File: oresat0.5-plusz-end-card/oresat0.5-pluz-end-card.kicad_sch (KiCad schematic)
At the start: 30 parts, among them J1 J-SAMTEC-TFM-120-01-L-D-RA, J2 Harwin M55-7101242R, J3 Harwin M55-7101242R, J4 Harwin M55-7101242R, J5 Harwin M55-7101242R, J6 Conn_Coaxial

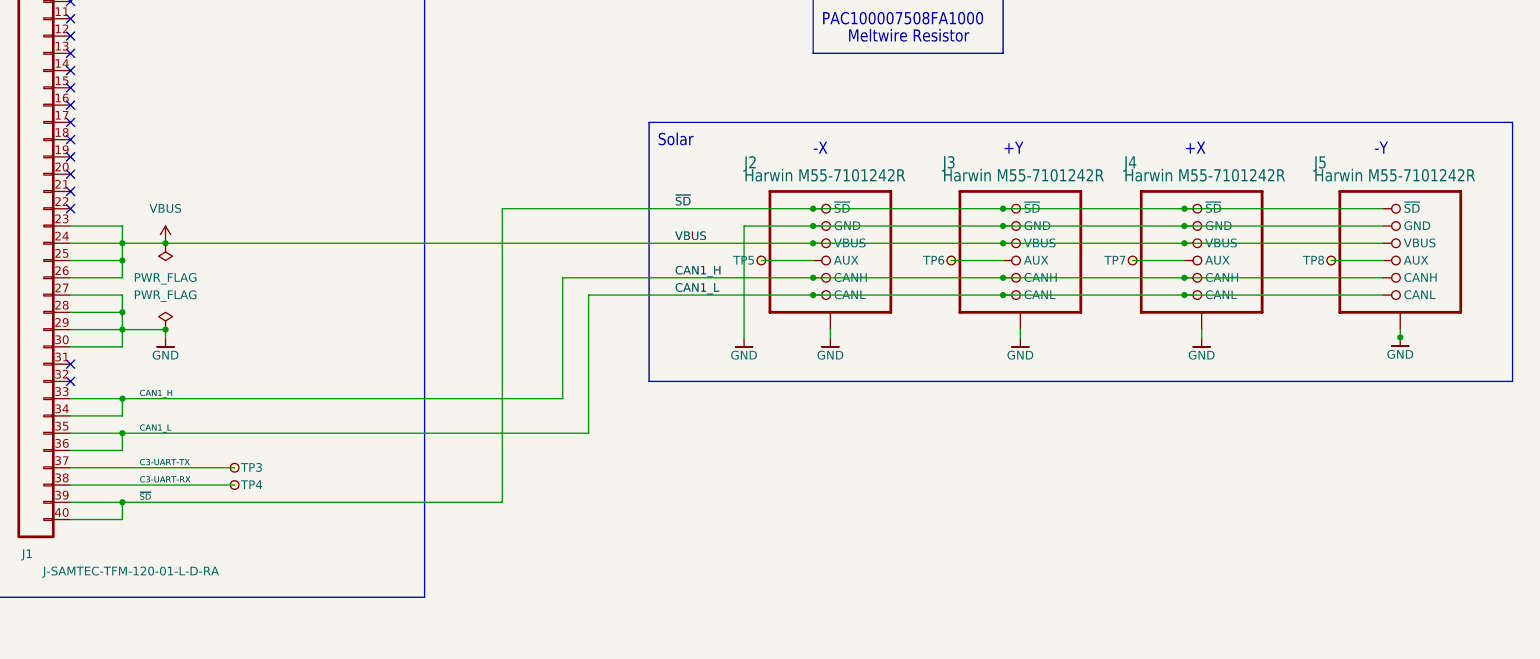
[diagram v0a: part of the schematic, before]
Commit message: Updated +Z end card connector symbols
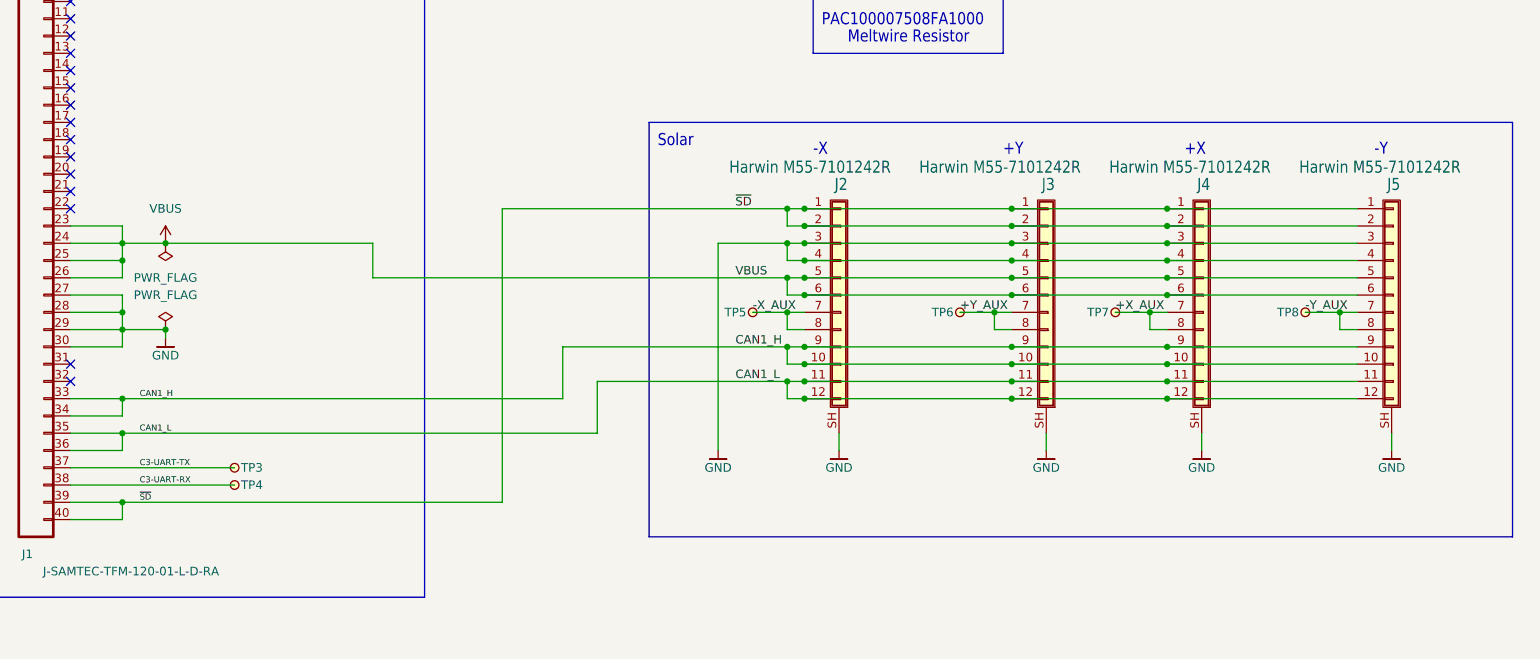
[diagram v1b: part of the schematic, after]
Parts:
- CF1: footprint plusz-end-card-with-turnstile:HARWIN-M55-60X1242R -> oresat-connectors:J-Harwin-M55-60X1242R; symbol plusz-end-card-with-turnstile-eagle-import:J-HARWIN-M55-60X1242R -> oresat-connectors:J-HARWIN-M55-6001242R
- J1: footprint oresat-footprints:J-SAMTEC-TFM-120-X1-XXX-D-RA -> oresat-connectors:J-SAMTEC-TFM-120-X1-XXX-D-RA
- J2, J3, J4, J5: footprint oresat-footprints:J-Harwin-M55-7101242R -> oresat-connectors:J-Harwin-M55-7101242R; symbol OreSat-j-solar-card-connector:SOLAR-CARD-CONNECTOR -> oresat-connectors:Harwin M55-7101242R
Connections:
- net GND: now also CF1.SH (SHIELD), J2.SH (Shield), J3.SH (Shield), J4.SH (Shield), J5.SH (Shield); no longer CF1.P$1 (SHIELDS), CF1.P$2 (SHIELDS), CF1.P$3 (SHIELDS), CF1.P$4 (SHIELDS), J2.GND (SHIELD), J3.GND (SHIELD), J4.GND (SHIELD), J5.GND (SHIELD)
- net -Y_AUX: now reaches J5.7 (Pin_7), J5.8 (Pin_8), TP8.1
- net +X_AUX: now reaches J4.7 (Pin_7), J4.8 (Pin_8), TP7.1
- net -X_AUX: now reaches J2.7 (Pin_7), J2.8 (Pin_8), TP5.1
- net +Y_AUX: now reaches J3.7 (Pin_7), J3.8 (Pin_8), TP6.1
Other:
- moved on the sheet: TP5, TP6, TP7, TP8

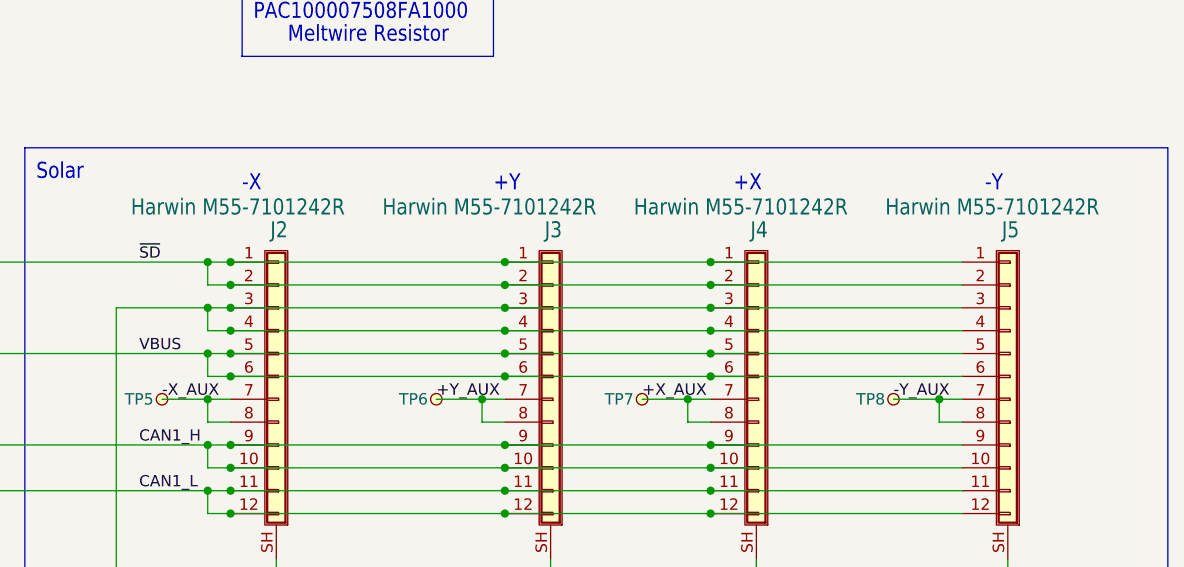
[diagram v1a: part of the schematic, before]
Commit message: Updated -Z end card and replaced eagle imported libraries with kicad libraries
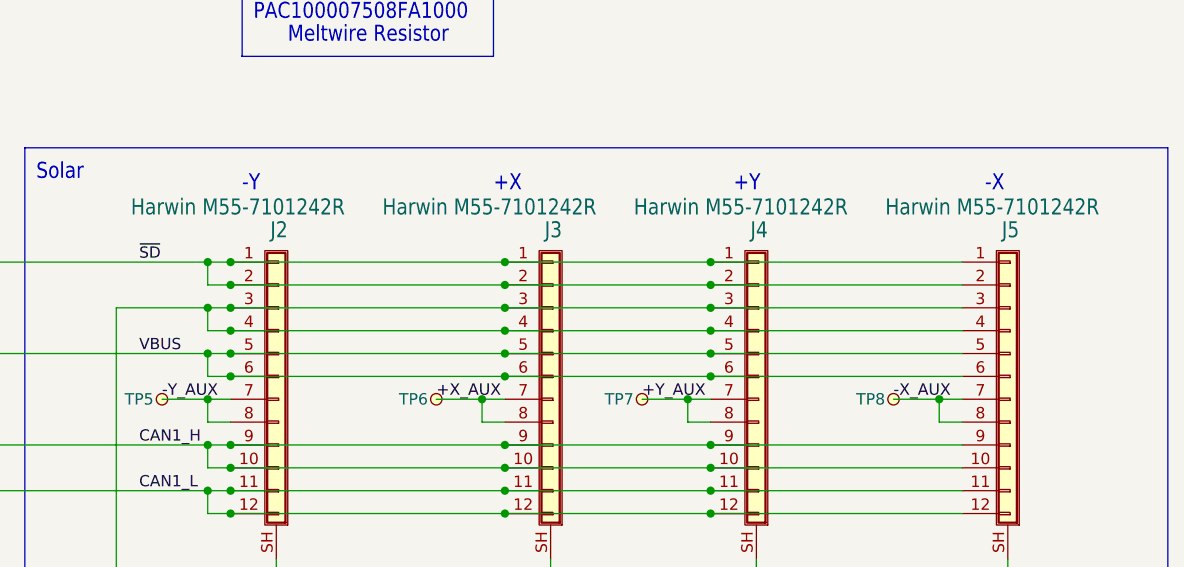
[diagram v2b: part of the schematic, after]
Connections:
- net +X_AUX: now also J3.7 (Pin_7), J3.8 (Pin_8), TP6.1; no longer J4.7 (Pin_7), J4.8 (Pin_8), TP7.1
- net +Y_AUX: now also J4.7 (Pin_7), J4.8 (Pin_8), TP7.1; no longer J3.7 (Pin_7), J3.8 (Pin_8), TP6.1
- net -X_AUX: now also J5.7 (Pin_7), J5.8 (Pin_8), TP8.1; no longer J2.7 (Pin_7), J2.8 (Pin_8), TP5.1
- net -Y_AUX: now also J2.7 (Pin_7), J2.8 (Pin_8), TP5.1; no longer J5.7 (Pin_7), J5.8 (Pin_8), TP8.1
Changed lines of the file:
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@@
     (effects (font (size 1.778 1.5113)) (justify left bottom))
   )
-  (text "-X" (at 176.53 142.24 180)
+  (text "-Y" (at 176.53 142.24 180)
     (effects (font (size 1.778 1.5113)) (justify left bottom))
   )
@@
     (effects (font (size 1.27 1.0795)) (justify left bottom))
   )
-  (text "-Y" (at 259.08 142.24 180)
+  (text "-X" (at 259.08 142.24 180)
     (effects (font (size 1.778 1.5113)) (justify left bottom))
   )
@@
     (effects (font (size 1.27 1.0795)) (justify left bottom))
   )
-  (text "+X" (at 231.14 142.24 180)
+  (text "+Y" (at 231.14 142.24 180)
     (effects (font (size 1.778 1.5113)) (justify left bottom))
   )
-  (text "+Y" (at 204.47 142.24 180)
+  (text "+X" (at 204.47 142.24 180)
     (effects (font (size 1.778 1.5113)) (justify left bottom))
   )
@@
     (effects (font (size 1.2446 1.2446)) (justify left bottom))
   )
-  (label "+Y_AUX" (at 198.12 165.1 0)
+  (label "+X_AUX" (at 198.12 165.1 0)
     (effects (font (size 1.27 1.27)) (justify left bottom))
   )
@@
     (effects (font (size 0.889 0.889)) (justify left bottom))
   )
-  (label "-X_AUX" (at 167.64 165.1 0)
+  (label "-Y_AUX" (at 167.64 165.1 0)
     (effects (font (size 1.27 1.27)) (justify left bottom))
   )
@@
     (effects (font (size 1.2446 1.2446)) (justify left bottom))
   )
-  (label "-Y_AUX" (at 248.92 165.1 0)
+  (label "-X_AUX" (at 248.92 165.1 0)
     (effects (font (size 1.27 1.27)) (justify left bottom))
   )
@@
     (effects (font (size 0.889 0.889)) (justify left bottom))
   )
-  (label "+X_AUX" (at 220.98 165.1 0)
+  (label "+Y_AUX" (at 220.98 165.1 0)
     (effects (font (size 1.27 1.27)) (justify left bottom))
   )

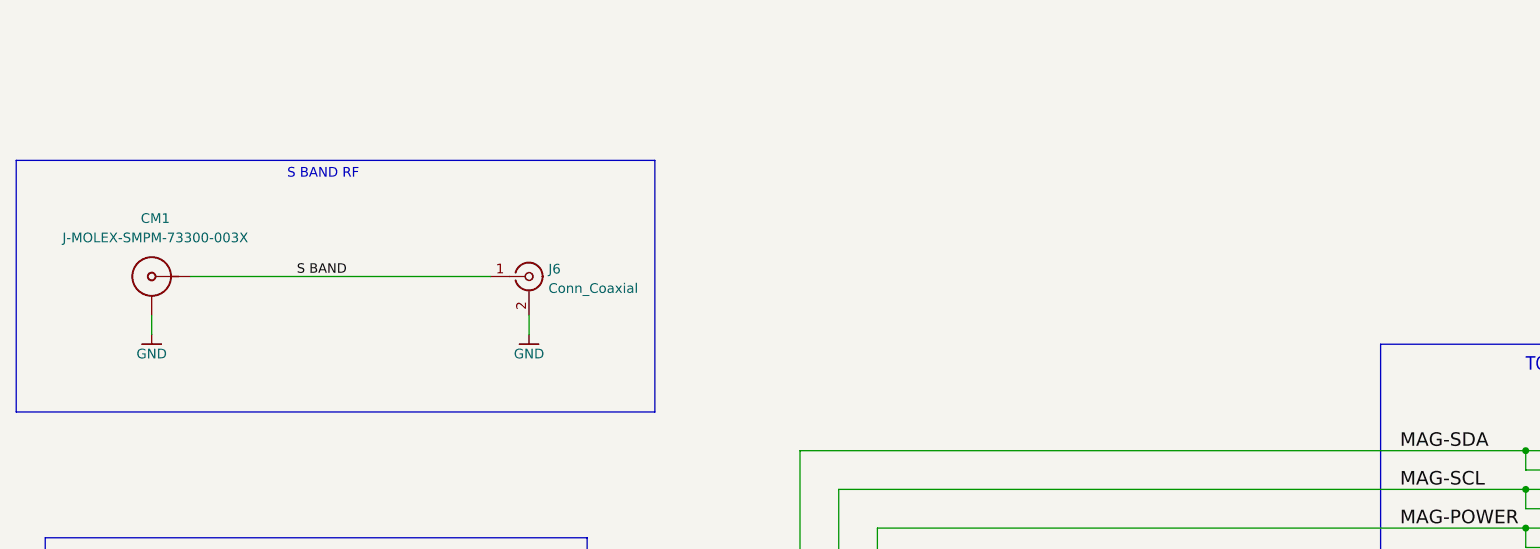
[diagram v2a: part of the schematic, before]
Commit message: Added helical landing pad and left hopefully enough room for Garrett to put in matching components.
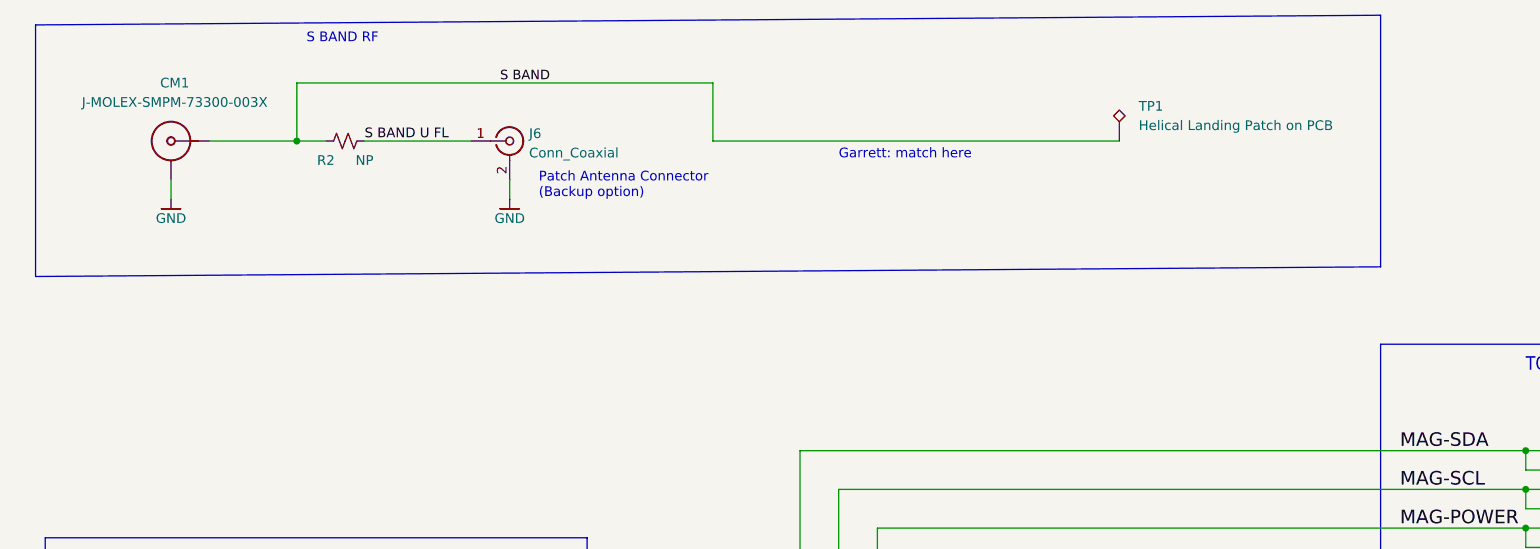
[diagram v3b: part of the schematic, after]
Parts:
- added R2: NP, Resistor_SMD:R_0402_1005Metric, symbol Device:R_Small_US
- added TP1: Helical Landing Patch on PCB, TestPoint:TestPoint_Pad_2.5x2.5mm, symbol Connector:TestPoint_Alt
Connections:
- net S BAND: now also R2.1, TP1.1; no longer J6.1 (In)
- new net S BAND U FL: J6.1 (In), R2.2
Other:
- note added: "Garrett: match here"
- note added: "Patch Antenna Connector (Backup option)"
- moved on the sheet: CM1, J6

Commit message: added Matching Components
Added matching components for s band antenna, ground stitching
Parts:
- added C1: C, Capacitor_SMD:C_0402_1005Metric, symbol Device:C
- added L1: L, Inductor_SMD:L_0402_1005Metric, symbol Device:L
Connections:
- net GND: now also L1.2
- net S BAND: now also C1.1; no longer TP1.1
- new net: C1.2, L1.1, TP1.1
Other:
- note added: "Inital L is 6.8nF, C is 1pF"
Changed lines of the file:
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@@
   (junction (at 205.74 172.72) (diameter 0) (color 0 0 0 0)
+  )
+  (junction (at 161.29 36.83) (diameter 0) (color 0 0 0 0)
   )
   (junction (at 175.26 160.02) (diameter 0) (color 0 0 0 0)
@@
     (stroke (width 0) (type default) (color 0 0 0 0))
   )
-  (wire (pts (xy 189.23 36.83) (xy 135.89 36.83))
+  (wire (pts (xy 161.29 36.83) (xy 189.23 36.83))
     (stroke (width 0) (type default) (color 0 0 0 0))
   )
@@
     (stroke (width 0) (type default) (color 0 0 0 0))
   )
+  (wire (pts (xy 158.75 36.83) (xy 161.29 36.83))
+    (stroke (width 0) (type default) (color 0 0 0 0))
+  )
   (polyline (pts (xy 152.4 137.16) (xy 152.4 198.12))
     (stroke (width 0) (type default) (color 0 0 0 0))
@@
   )
   (wire (pts (xy 172.72 160.02) (xy 111.76 160.02))
+    (stroke (width 0) (type default) (color 0 0 0 0))
+  )
+  (wire (pts (xy 135.89 36.83) (xy 151.13 36.83))
     (stroke (width 0) (type default) (color 0 0 0 0))
   )
@@
     (effects (font (size 1.27 1.0795)) (justify left bottom))
   )
+  (text "Inital L is 6.8nF, C is 1pF" (at 160.655 33.655 0)
+    (effects (font (size 1.27 1.27)) (justify left bottom))
+  )
   (text "Meltwire Resistor" (at 181.61 125.73 180)
     (effects (font (size 1.778 1.5113)) (justify left bottom))
   )
-  (text "Garrett: match here" (at 152.4 39.37 0)
+  (text "Garrett: match here" (at 156.845 51.435 0)
     (effects (font (size 1.27 1.27)) (justify left bottom))
   )
@@
     )
   )
+  (symbol (lib_id "Device:C") (at 154.94 36.83 90) (unit 1)
+    (in_bom yes) (on_board yes) (fields_autoplaced)
+    (property "Reference" "C1" (id 0) (at 154.94 29.21 90))
+    (property "Value" "C" (id 1) (at 154.94 31.75 90))
+    (property "Footprint" "Capacitor_SMD:C_0402_1005Metric" (id 2) (at 158.75 35.8648 0)
+      (effects (font (size 1.27 1.27)) hide)
+    )
+    (property "Datasheet" "~" (id 3) (at 154.94 36.83 0)
+      (effects (font (size 1.27 1.27)) hide)
+    )
+    (pin "1")
+    (pin "2")
+  )
   (symbol (lib_id "oresat-misc:TestPoint-MinTH") (at 248.92 165.1 270) (unit 1)
     (in_bom yes) (on_board yes)
@@
     (pin "1")
   )
+  (symbol (lib_id "oresat-power:GND") (at 161.29 44.45 0) (unit 1)
+    (in_bom yes) (on_board yes)
+    (property "Reference" "#GND0105" (id 0) (at 161.29 50.8 0)
+      (effects (font (size 1.27 1.27)) hide)
+    )
+    (property "Value" "GND" (id 1) (at 161.29 46.99 0))
+    (property "Footprint" "" (id 2) (at 161.29 44.45 0)
+      (effects (font (size 1.27 1.27)) hide)
+    )
+    (property "Datasheet" "" (id 3) (at 161.29 44.45 0)
+      (effects (font (size 1.27 1.27)) hide)
+    )
+    (pin "1")
+  )
   (symbol (lib_id "oresat-power:GND") (at 109.22 44.45 0) (unit 1)
     (in_bom yes) (on_board yes)
@@
       (effects (font (size 1.27 1.27)) hide)
     )
+  )
+  (symbol (lib_id "Device:L") (at 161.29 40.64 0) (unit 1)
+    (in_bom yes) (on_board yes) (fields_autoplaced)
+    (property "Reference" "L1" (id 0) (at 162.56 39.3699 0)
+      (effects (font (size 1.27 1.27)) (justify left))
+    )
+    (property "Value" "L" (id 1) (at 162.56 41.9099 0)
+      (effects (font (size 1.27 1.27)) (justify left))
+    )
+    (property "Footprint" "Inductor_SMD:L_0402_1005Metric" (id 2) (at 161.29 40.64 0)
+      (effects (font (size 1.27 1.27)) hide)
+    )
+    (property "Datasheet" "~" (id 3) (at 161.29 40.64 0)
+      (effects (font (size 1.27 1.27)) hide)
+    )
+    (pin "1")
+    (pin "2")
   )
   (symbol (lib_id "oresat-connectors:J-HARWIN-M55-6001242R") (at 252.73 90.17 0) (unit 1)
@@
       (reference "#GND0104") (unit 1) (value "GND") (footprint "")
     )
+    (path "/437e85ba-ae7f-4ed0-9fc9-8ac0e7991c2d"
+      (reference "#GND0105") (unit 1) (value "GND") (footprint "")
+    )
     (path "/0795f37d-e1f5-48cc-ab01-8a3be26e7bbf"
       (reference "#VBUS01") (unit 1) (value "VBUS") (footprint "")
     )
+    (path "/21c5f26e-c09a-4a8f-9b83-fb665500858e"
+      (reference "C1") (unit 1) (value "C") (footprint "Capacitor_SMD:C_0402_1005Metric")
+    )
     (path "/537f3fbf-459d-46ae-b76a-237157a04de5"
       (reference "CF1") (unit 1) (value "J-HARWIN-M55-6001242R") (footprint "oresat-connectors:J-Harwin-M55-60X1242R")
@@
       (reference "J6") (unit 1) (value "Conn_Coaxial") (footprint "Connector_Coaxial:U.FL_Hirose_U.FL-R-SMT-1_Vertical")
     )
+    (path "/52a8c9dc-c5aa-485c-817d-caad5d80c397"
+      (reference "L1") (unit 1) (value "L") (footprint "Inductor_SMD:L_0402_1005Metric")
+    )
     (path "/0cc9f9e8-5bbb-4a89-9332-5d6156333b7c"
